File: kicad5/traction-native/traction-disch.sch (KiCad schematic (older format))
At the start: 35 parts

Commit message: Rev A.16: round 17 — gap closure (F174-F189) + round 16 rev A.15 (F167-F173): every gap closed, upgraded or numbered
Round 16 (rev A.15, three rechecks of 32214be): exciter MFB gain 24 k -> 28 k with the amplitude
planes (setpoint 7.2 V pp at the monitor), unidirectional exciter TVS, /33X hold 0.07 A, firmware
acquisition contracts (phase triplets, resolver frame age, coherent SDADC frames); BOM furnished
(spec-class capacitors, drawn-size gate in bom-gen, last placeholders bound with archived sheets).

Round 17 (rev A.16, "close all gaps" / "feel free to upgrade"):
- Hardware: DEXP/DEXN PMEG4050EP-Q rated back-drive diversion (closes the ALM2402 OPEN row);
  exciter TVS -> SMDJ8.5A-HRA (3 kW, AEC-Q101, same pad); fault rows split single fault (PASS
  at any source impedance) vs load-dump-coincident double event; LV entry re-designed as
  LET-THROUGH for ISO 16750-2 test B (TPSMC33A-VR/TPSMC18A-VR anti-series pair at the pin ahead
  of the reverse Schottky, TPSMC33CA-VR on the power board, CLVC3 100 uF hybrid polymer, FLVC
  5 A fuse, DIGN US1M, ULDO15 D2PAK) — pulse 1 was avalanching DREVC, the 2023 26 V jump start
  opened the old TVS, the polyfuse was undersized at 9 V; RFS4 -> ESR18 1206.
- Stale/unsourced rows recomputed: cold-crank excitation, PTC hold (IR-13), discharge resistor
  no-flame statement, hall reference drift, ASC command-path collapse.
- KiCad: a KiCad 9/10 set (kicad/traction, Traction-Inverter-KiCad-modern.zip) proved by
  kicad-cli netlist export on every board with mutation tests; KiCad 10 cannot resolve the KiCad 5
  legacy symbols; the proof exposed harness pins numbered P1-P40 and the SMDJ drawn as a resistor
  in the legacy generator — fixed; sym-lib-table + cache library in both legacy sets.
- Firmware: all 35 open contract items closed (FW-08 zero-current decision, FW-31 liveness,
  FW-32 UDS service-lock routine, FW-33 supply-overvoltage supervision), FS26 watchdog answer
  3.0 ms -> 2.0 ms, ASC-exit release wait CAL, 39-row silicon/RM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
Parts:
- JCTL: value HDR-1x4-2.54 -> IPL1-104-01-L-S-K; footprint HDR1x4 -> IPL1-104 (1x4 2.54 mm THT); symbol traction-r1:HDR-1x4-2.54 -> traction-r1:IPL1-104-01-L-S-K; MPN HDR-1x4-2.54 -> IPL1-104-01-L-S-K
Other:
- note added: "220 kW pk Discharge (HV, bolt-on) - 3 of 4 · rev A.16 · 3 sections · 35 components"
- note removed: "220 kW pk Discharge (HV, bolt-on) - 3 of 4 · rev A.14 · 3 sections · 35 components"
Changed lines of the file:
@@
 Title "Traction Inverter — Discharge board (bolt-on, XM3 pattern)"
 Date "2026-09-23"
-Rev "A.14"
+Rev "A.16"
 Comp "Traction Inverter 220 kW pk - Discharge (HV, bolt-on), sheet 3 of 4"
 Comment1 "Inverter = Power board + Cap bank busbar + bolt-on Discharge board (all HV) + Control card (LV); safe state holds with any link lost"
@@
 $EndDescr
 Text Notes 600 7600 0    60   ~ 12
-220 kW pk Discharge (HV, bolt-on) - 3 of 4   ·   rev A.14   ·   3 sections   ·   35 components
+220 kW pk Discharge (HV, bolt-on) - 3 of 4   ·   rev A.16   ·   3 sections   ·   35 components
 Text Notes 600 7900 0    50   ~ 0
 NET NAMING: U<ref>_<PIN> = node at that IC pin   ·   R<stem>_M = series-pair midpoint   ·   R<stem>_<nm> = tap between R<stem>n/m   ·   all others are explicit design nets   ·   same name on another sheet = same net, joined only at the named connector/stud/tab
@@
 DISCHARGE / ENTRY
 $Comp
-L traction-r1:HDR-1x4-2.54 JCTL
+L traction-r1:IPL1-104-01-L-S-K JCTL
 U 1 1 5E00015F
 P 9150 5850
 F 0 "JCTL" H 8750 5550 50  0000 R CNN
-F 1 "HDR-1x4-2.54" H 8750 6180 50  0000 R CNN
-F 2 "HDR1x4" H 9150 5850 50  0001 C CNN
+F 1 "IPL1-104-01-L-S-K" H 8750 6180 50  0000 R CNN
+F 2 "IPL1-104 (1x4 2.54 mm THT)" H 9150 5850 50  0001 C CNN
 F 3 "~" H 9150 5850 50  0001 C CNN
 F 4 "CLASS" H 9150 5850 50  0001 C CNN "LCSC"
-F 5 "HDR-1x4-2.54" H 9150 5850 50  0001 C CNN "MPN"
+F 5 "IPL1-104-01-L-S-K" H 9150 5850 50  0001 C CNN "MPN"
 	1    9150 5850
 	1    0    0    -1

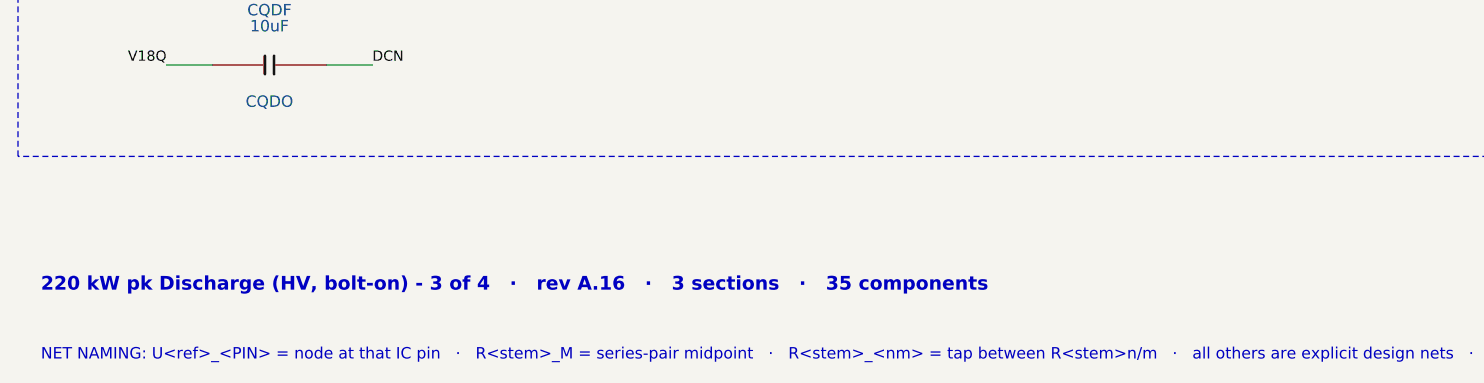
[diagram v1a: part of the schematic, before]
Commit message: Rev A.17: round 18 — three rechecks of 4425af9 (F190-F198): diversion diodes on the amplifier node (loop passes RSX), diode cell cathode = pin 1 on all 35 diodes, exciter TVS/PTC rows at worst corners + ECU-asleep sustained short (WARN rows, layout rule, QP-RX-04 2b gate), anti-surge RSX, NCV4276C reverse current = QP-RX-05 gate + VR-33, IR-16/IR-42, firmware FW-34..36 (sample freshness, cadence-locked resolver frames, latency sign) + three self-found instances
Co-Authored-By: Claude Fable 5.1 <noreply@anthropic.com>
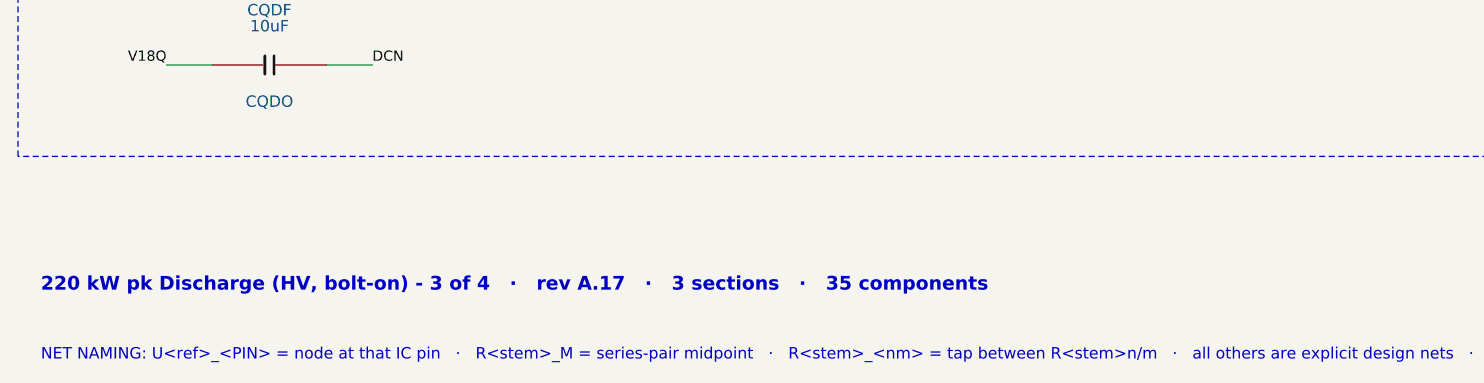
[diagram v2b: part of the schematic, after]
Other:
- note added: "220 kW pk Discharge (HV, bolt-on) - 3 of 4 · rev A.17 · 3 sections · 35 components"
- note removed: "220 kW pk Discharge (HV, bolt-on) - 3 of 4 · rev A.16 · 3 sections · 35 components"
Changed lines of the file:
@@
 Title "Traction Inverter — Discharge board (bolt-on, XM3 pattern)"
 Date "2026-09-23"
-Rev "A.16"
+Rev "A.17"
 Comp "Traction Inverter 220 kW pk - Discharge (HV, bolt-on), sheet 3 of 4"
 Comment1 "Inverter = Power board + Cap bank busbar + bolt-on Discharge board (all HV) + Control card (LV); safe state holds with any link lost"
@@
 $EndDescr
 Text Notes 600 7600 0    60   ~ 12
-220 kW pk Discharge (HV, bolt-on) - 3 of 4   ·   rev A.16   ·   3 sections   ·   35 components
+220 kW pk Discharge (HV, bolt-on) - 3 of 4   ·   rev A.17   ·   3 sections   ·   35 components
 Text Notes 600 7900 0    50   ~ 0
 NET NAMING: U<ref>_<PIN> = node at that IC pin   ·   R<stem>_M = series-pair midpoint   ·   R<stem>_<nm> = tap between R<stem>n/m   ·   all others are explicit design nets   ·   same name on another sheet = same net, joined only at the named connector/stud/tab

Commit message: Rev A.18: round 19 — three rechecks of e315bf1 (F199-F204): PTC-current row at every permitted voltage (IR-16 0.08/0.14/0.37/0.26 Ω), ≥8 A TVS energy an explicit assumption + QP-RX-04 release criterion, window criterion fixed, exciter TVS → SMDJ7.0A-HRA (coupled island holds the 7.0 V class at a parked 12 V battery / the Marine rail), shared exciter-fault model run for the Marine port (QP-MA-11, kit-loom rule), FW-35 rewritten on an SWG-anchored time origin with clock-derived resync and bounded restart
Co-Authored-By: Claude Fable 5.1 <noreply@anthropic.com>
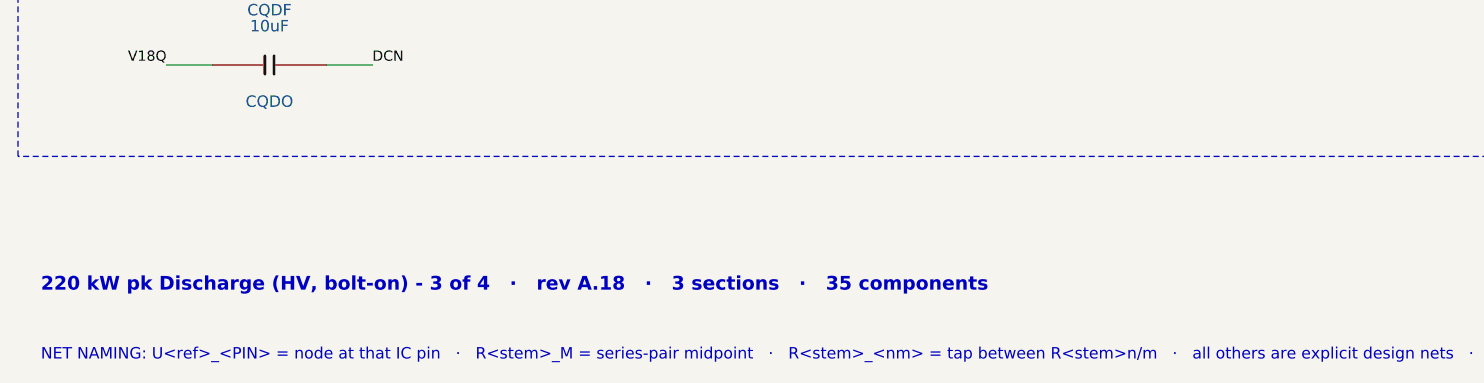
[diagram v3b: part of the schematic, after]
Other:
- note added: "220 kW pk Discharge (HV, bolt-on) - 3 of 4 · rev A.18 · 3 sections · 35 components"
- note removed: "220 kW pk Discharge (HV, bolt-on) - 3 of 4 · rev A.17 · 3 sections · 35 components"
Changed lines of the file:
@@
 Title "Traction Inverter — Discharge board (bolt-on, XM3 pattern)"
 Date "2026-09-23"
-Rev "A.17"
+Rev "A.18"
 Comp "Traction Inverter 220 kW pk - Discharge (HV, bolt-on), sheet 3 of 4"
 Comment1 "Inverter = Power board + Cap bank busbar + bolt-on Discharge board (all HV) + Control card (LV); safe state holds with any link lost"
@@
 $EndDescr
 Text Notes 600 7600 0    60   ~ 12
-220 kW pk Discharge (HV, bolt-on) - 3 of 4   ·   rev A.17   ·   3 sections   ·   35 components
+220 kW pk Discharge (HV, bolt-on) - 3 of 4   ·   rev A.18   ·   3 sections   ·   35 components
 Text Notes 600 7900 0    50   ~ 0
 NET NAMING: U<ref>_<PIN> = node at that IC pin   ·   R<stem>_M = series-pair midpoint   ·   R<stem>_<nm> = tap between R<stem>n/m   ·   all others are explicit design nets   ·   same name on another sheet = same net, joined only at the named connector/stud/tab

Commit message: Rev A.19: round 20 — three rechecks of 00f6252 (F205-F207): TVS alternate to the 7.0 V class + lock, 4XX discharge alternate 470→220 Ω + lock, T-05/T-06 firmware ID, 8.5 V-era figures re-derived at the IR-16 allocations
Co-Authored-By: Claude Fable 5.1 <noreply@anthropic.com>
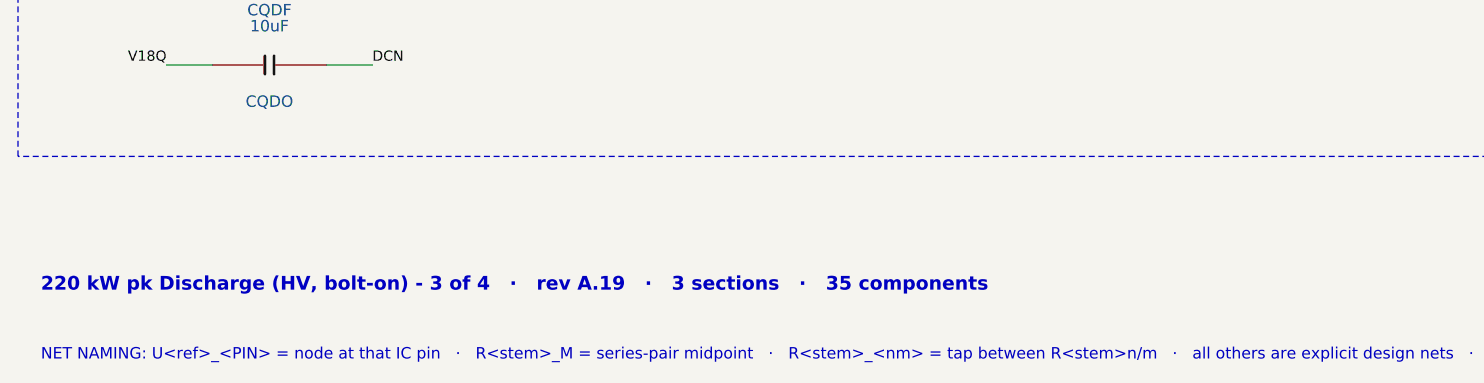
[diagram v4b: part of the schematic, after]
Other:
- note added: "220 kW pk Discharge (HV, bolt-on) - 3 of 4 · rev A.19 · 3 sections · 35 components"
- note removed: "220 kW pk Discharge (HV, bolt-on) - 3 of 4 · rev A.18 · 3 sections · 35 components"
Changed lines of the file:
@@
 Title "Traction Inverter — Discharge board (bolt-on, XM3 pattern)"
 Date "2026-09-23"
-Rev "A.18"
+Rev "A.19"
 Comp "Traction Inverter 220 kW pk - Discharge (HV, bolt-on), sheet 3 of 4"
 Comment1 "Inverter = Power board + Cap bank busbar + bolt-on Discharge board (all HV) + Control card (LV); safe state holds with any link lost"
@@
 $EndDescr
 Text Notes 600 7600 0    60   ~ 12
-220 kW pk Discharge (HV, bolt-on) - 3 of 4   ·   rev A.18   ·   3 sections   ·   35 components
+220 kW pk Discharge (HV, bolt-on) - 3 of 4   ·   rev A.19   ·   3 sections   ·   35 components
 Text Notes 600 7900 0    50   ~ 0
 NET NAMING: U<ref>_<PIN> = node at that IC pin   ·   R<stem>_M = series-pair midpoint   ·   R<stem>_<nm> = tap between R<stem>n/m   ·   all others are explicit design nets   ·   same name on another sheet = same net, joined only at the named connector/stud/tab

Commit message: Rev A.20: round 21 — three rechecks of 551c405 (F208): stale 0.29 Ω in gate ㉘ and the QP-RX-04 fixture instruction → 0.37 Ω, last 8.5 V-era figures aligned, Marine sweep cross-references at the current values
Co-Authored-By: Claude Fable 5.1 <noreply@anthropic.com>
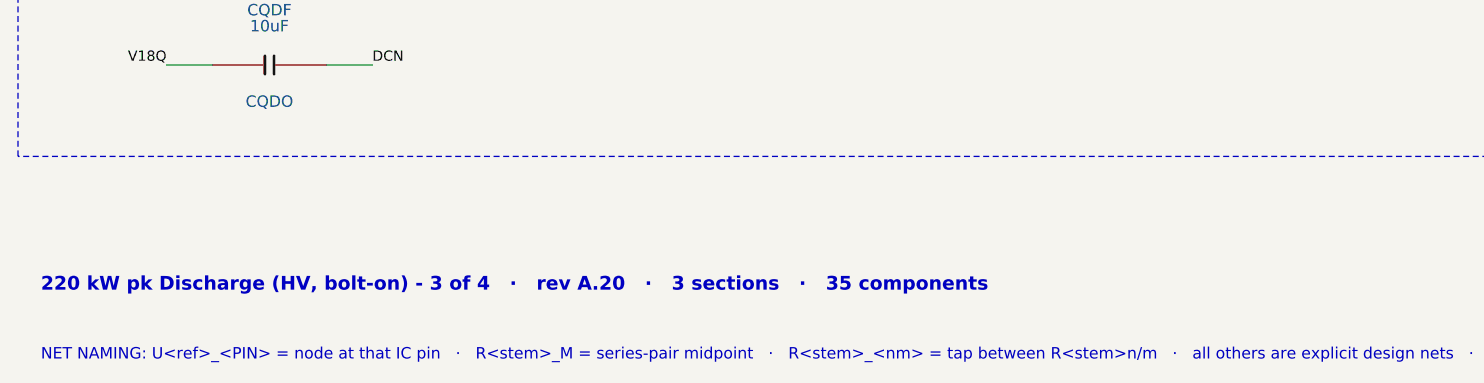
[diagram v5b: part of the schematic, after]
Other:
- note added: "220 kW pk Discharge (HV, bolt-on) - 3 of 4 · rev A.20 · 3 sections · 35 components"
- note removed: "220 kW pk Discharge (HV, bolt-on) - 3 of 4 · rev A.19 · 3 sections · 35 components"
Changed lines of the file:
@@
 Title "Traction Inverter — Discharge board (bolt-on, XM3 pattern)"
 Date "2026-09-23"
-Rev "A.19"
+Rev "A.20"
 Comp "Traction Inverter 220 kW pk - Discharge (HV, bolt-on), sheet 3 of 4"
 Comment1 "Inverter = Power board + Cap bank busbar + bolt-on Discharge board (all HV) + Control card (LV); safe state holds with any link lost"
@@
 $EndDescr
 Text Notes 600 7600 0    60   ~ 12
-220 kW pk Discharge (HV, bolt-on) - 3 of 4   ·   rev A.19   ·   3 sections   ·   35 components
+220 kW pk Discharge (HV, bolt-on) - 3 of 4   ·   rev A.20   ·   3 sections   ·   35 components
 Text Notes 600 7900 0    50   ~ 0
 NET NAMING: U<ref>_<PIN> = node at that IC pin   ·   R<stem>_M = series-pair midpoint   ·   R<stem>_<nm> = tap between R<stem>n/m   ·   all others are explicit design nets   ·   same name on another sheet = same net, joined only at the named connector/stud/tab

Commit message: Rev A.21: round 22 — three rechecks of 0ff44d9 (F209) + the layout handoff (F210–F213): every KiCad symbol bound to a footprint in a shipped traction.pretty (45 verbatim KiCad-10 patterns + 18 datasheet-drawn), fp-lib-table and per-board projects in all sets, pad-per-pin KiCad proof; NCV4276C 5-lead lands, ALM2402/TPS55340 thermal-pad pins, 2-pad crystal; QP §0.2 baseline and stale IDs; docs/layout-handoff.md
Co-Authored-By: Claude Fable 5.1 <noreply@anthropic.com>
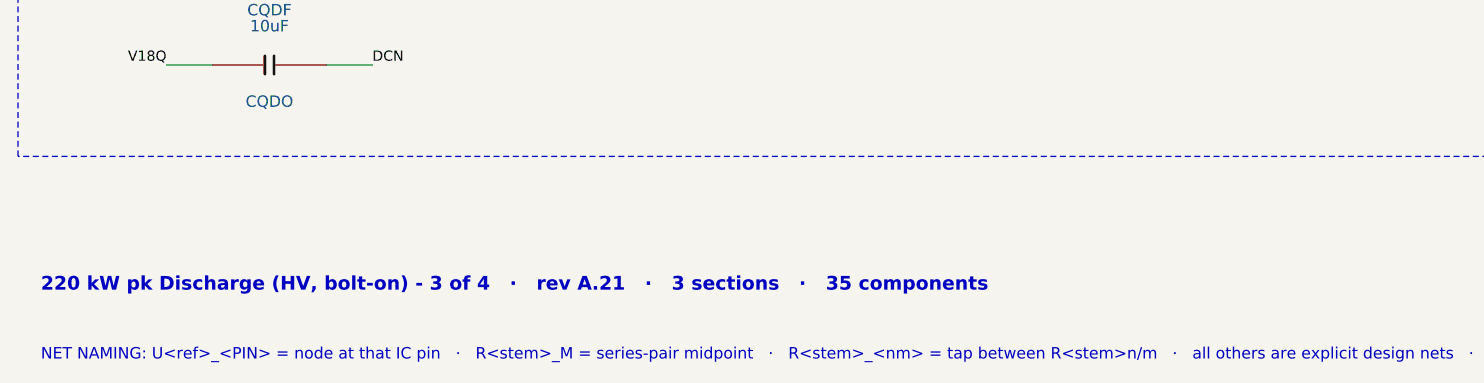
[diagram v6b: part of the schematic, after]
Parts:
- CQD, CQDF, CQDIB: footprint C0603 -> traction:C_0603_1608Metric
- CQDI1, CQDI2: footprint C1206 -> traction:C_1206_3216Metric
- CQDO: footprint C1210 -> traction:C_1210_3225Metric
- JCTL: footprint IPL1-104 (1x4 2.54 mm THT) -> traction:Samtec_IPL1-104_1x04
- JDCN, JDCP: footprint StudM6 -> traction:MountingHole_6.4mm_M6_Pad
- PSQD: footprint DWN36 -> traction:UCC14141-Q1_DWN36
- QDIS: footprint TO247-4L -> traction:TO-247-4_Vertical
- RBLD1, RBLD10, RBLD11, RBLD12, RBLD2, RBLD3, RBLD4, RBLD5, RBLD6, RBLD7, RBLD8, RBLD9: footprint R2512 -> traction:R_2512_6332Metric
- RDIS1, RDIS2, RDIS3, RDIS4: footprint AxialWW10W -> traction:Yageo_SQP10_P55.88
- RQDE1, RQDE2, RQDF1, RQDF2, RQDG, RQDL, RQDPD: footprint R0603 -> traction:R_0603_1608Metric
- UQD: footprint SMD8W -> traction:VOW3120_SMD8W
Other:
- note added: "220 kW pk Discharge (HV, bolt-on) - 3 of 4 · rev A.21 · 3 sections · 35 components"
- note removed: "220 kW pk Discharge (HV, bolt-on) - 3 of 4 · rev A.20 · 3 sections · 35 components"

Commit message: Rev A.22: round 23 — rechecks of 452de85 (F214–F220), the VESC program (FW-38…FW-46, Traction Tool in Qt) and the "why not done" extension (F221–F239)
Hardware: the R2R reference isolated at ball A9 (RR2R 10 Ω + 1 µF + 100 nF, S32K39 DS note 8), the SWD header on its
surface-mount Samtec land with a mounting-technology lock in the library generator, the footprint library declared
KiCad 10.0.6+ and no longer mirrored into the KiCad 5 sets; the BOM intro follows the SKU; a VREFH window row and VR-34/35.

Firmware (TI_FW_ID 0x0A0F0015, CAL layout 4, 190 fields / 91 CAL rows, 80 DTCs): FW-37 joint torque solve with a
postcondition; the VESC gap closure — FW-38 signed field update (Ed25519, anti-rollback, ISO-TP), FW-39 interlocked motor
self-commissioning, FW-40 UDS diagnostics (0x19/0x22/0x2A/0x14 over ISO 15765-2), FW-41 fault-triggered waveform capture,
FW-42 overspeed, FW-43 run-time statistics, FW-44 key-on offset adoption, FW-45 saturation-dependent inductance tables
with gain scheduling, FW-46 cogging feed-forward; twelve defects found by the closed-loop simulator bridge (F221–F232),
the 64-bit divide out of every ISR path with a link-time guard, the UDS escape single frame accepted by every service,
the root of trust reported (DID 0xFD23), the boot record, motor data and active maps as DIDs; 421 tests / 4937 checks /
0 failed on the host (-O1, -O2, ASan/UBSan, -ffp-contract=off) and on the Cortex-M7 under QEMU with the target compiler
(make qemu-test, T-59); make target-check 63 markers, make target-size with the divide guard.

Traction Tool (tool/): Qt 6 / C++17 Widgets + Qwt, offline; pages Dashboard, Live plots, Controls, Commissioning,
Parameters, Faults & alerts, Analysis, Terminal, Firmware; transports simulator bridge (tool/bridge, the real firmware
against a plant), log replay, CAN (QCanBus with ISO-TP both ways, proved against the firmware over the virtualcan bus);
the signed update end to end over both transports; the commissioning routines, the map sw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
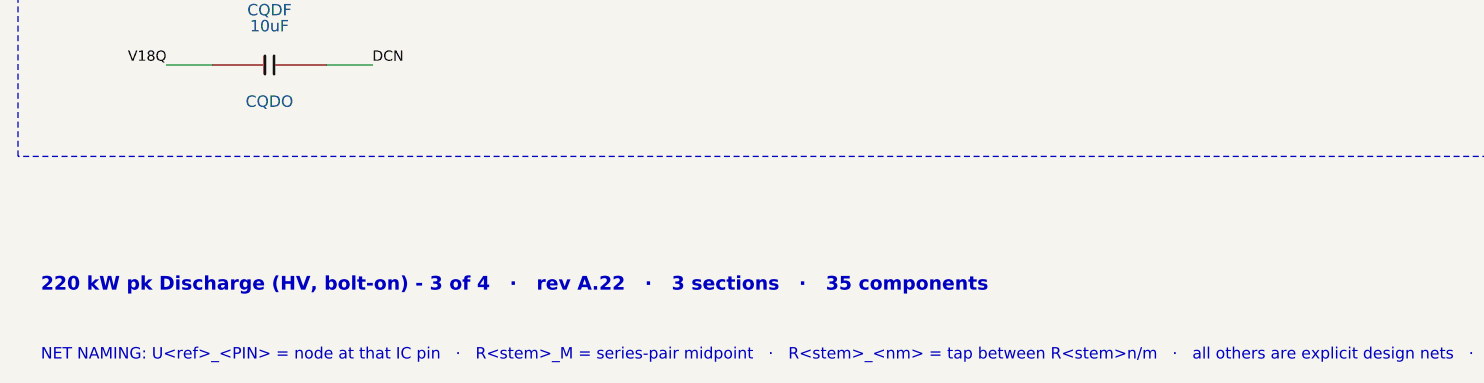
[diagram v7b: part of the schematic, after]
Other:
- note added: "220 kW pk Discharge (HV, bolt-on) - 3 of 4 · rev A.22 · 3 sections · 35 components"
- note removed: "220 kW pk Discharge (HV, bolt-on) - 3 of 4 · rev A.21 · 3 sections · 35 components"
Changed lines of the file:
@@
 Title "Traction Inverter — Discharge board (bolt-on, XM3 pattern)"
 Date "2026-09-23"
-Rev "A.21"
+Rev "A.22"
 Comp "Traction Inverter 220 kW pk - Discharge (HV, bolt-on), sheet 3 of 4"
 Comment1 "Inverter = Power board + Cap bank busbar + bolt-on Discharge board (all HV) + Control card (LV); safe state holds with any link lost"
@@
 $EndDescr
 Text Notes 600 7600 0    60   ~ 12
-220 kW pk Discharge (HV, bolt-on) - 3 of 4   ·   rev A.21   ·   3 sections   ·   35 components
+220 kW pk Discharge (HV, bolt-on) - 3 of 4   ·   rev A.22   ·   3 sections   ·   35 components
 Text Notes 600 7900 0    50   ~ 0
 NET NAMING: U<ref>_<PIN> = node at that IC pin   ·   R<stem>_M = series-pair midpoint   ·   R<stem>_<nm> = tap between R<stem>n/m   ·   all others are explicit design nets   ·   same name on another sheet = same net, joined only at the named connector/stud/tab
